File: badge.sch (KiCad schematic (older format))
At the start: 39 parts, among them J1 DevKitC_L, J10 HT024SQV003NH, J11 EXT3, J2 DevKitC_R, J3 HT024SQV010NH, J4 EXT1_1, J5 EXT1_2, J6 EXT1_3, J7 EXT2_1, J8 EXT2_2, J9 EXT2_3, SW1 UP, SW2 LEFT, SW3 A, SW4 DOWN, SW5 RIGHT, SW6 B, SW7 SW_DIP_x03, U1 ESP32-DEVKITC-32D

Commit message: Vertical badge style
* Change C9 footprint to 2816
* Add 3D model for 5 wat tactile switch
* 3D models should be located in ${HOME}/kicad/template
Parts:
- added J13: DevKitC_R_SMD, Connector_PinSocket_2.54mm:PinSocket_1x19_P2.54mm_Vertical_SMD_Pin1Left, symbol Connector:Conn_01x19_Female
- C9: value 0603/220uF/16V -> 2917/220uF/16V; footprint Capacitor_SMD:C_0603_1608Metric -> Capacitor_SMD:C_2816_7142Metric
- SW7: footprint custom_footprint:ITS-1500S -> custom_footprint:ITS-1500S-A
- gave numbers to parts that had none: 1
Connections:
- net GND: now also J13.1 (Pin_1), J13.7 (Pin_7)
- net GPIO15: now also J13.16 (Pin_16)
- net GPIO16: now also J13.12 (Pin_12)
- net GPIO17: now also J13.11 (Pin_11)
- net GPIO2: now also J13.15 (Pin_15)
- net GPIO4: now also J13.13 (Pin_13)
- net LCD_DC: now also J13.3 (Pin_3)
- net LCD_RST: now also J13.6 (Pin_6)
- net VSPI_CS: now also J13.10 (Pin_10)
- net VSPI_MISO: now also J13.8 (Pin_8)
- net VSPI_MOSI: now also J13.2 (Pin_2)
- net VSPI_SCK: now also J13.9 (Pin_9)
- no-connect marks 77 -> 83
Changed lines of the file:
@@
 	5800 500  5800 3200
-Wire Notes Line
-	4100 3200 500  3200
 Wire Notes Line
 	500  3200 500  500
@@
 P 9000 5900
 F 0 "C9" V 8900 5950 50  0000 C CNN
-F 1 "0603/220uF/16V" V 8900 5500 50  0000 C CNN
-F 2 "Capacitor_SMD:C_0603_1608Metric" H 9000 5900 50  0001 C CNN
+F 1 "2917/220uF/16V" V 8900 5500 50  0000 C CNN
+F 2 "Capacitor_SMD:C_2816_7142Metric" H 9000 5900 50  0001 C CNN
 F 3 "~" H 9000 5900 50  0001 C CNN
 	1    9000 5900
@@
 F 0 "SW7" H 4800 5667 50  0000 C CNN
 F 1 "SW_DIP_x03" H 4800 5576 50  0000 C CNN
-F 2 "custom_footprint:ITS-1500S" H 4800 5200 50  0001 C CNN
+F 2 "custom_footprint:ITS-1500S-A" H 4800 5200 50  0001 C CNN
 F 3 "" H 4800 5200 50  0001 C CNN
 	1    4800 5200
@@
 GPIO39
 $Comp
-L Connector:Conn_01x19_Female J?
+L Connector:Conn_01x19_Female J12
 U 1 1 5C04F616
 P 1300 2000
-F 0 "J?" H 1200 3100 50  0000 L CNN
+F 0 "J12" H 1200 3100 50  0000 L CNN
 F 1 "DevKitC_L_SMD" H 1000 3000 50  0000 L CNN
 F 2 "Connector_PinSocket_2.54mm:PinSocket_1x19_P2.54mm_Vertical_SMD_Pin1Right" H 1300 2000 50  0001 C CNN
@@
 NoConn ~ 1100 2600
 $Comp
-L power:+5V #PWR?
+L power:+5V #PWR0117
 U 1 1 5C04F61F
 P 900 2900
-F 0 "#PWR?" H 900 2750 50  0001 C CNN
+F 0 "#PWR0117" H 900 2750 50  0001 C CNN
 F 1 "+5V" H 915 3073 50  0000 C CNN
 F 2 "" H 900 2900 50  0001 C CNN
@@
 GPIO34
 $Comp
-L power:GND #PWR?
+L power:GND #PWR0118
 U 1 1 5C04F628
 P 700 2400
-F 0 "#PWR?" H 700 2150 50  0001 C CNN
+F 0 "#PWR0118" H 700 2150 50  0001 C CNN
 F 1 "GND" H 705 2227 50  0000 C CNN
 F 2 "" H 700 2400 50  0001 C CNN
@@
 	700  2400 1100 2400
 $Comp
-L power:+3.3V #PWR?
+L power:+3.3V #PWR0119
 U 1 1 5C04F62F
 P 700 1100
-F 0 "#PWR?" H 700 950 50  0001 C CNN
+F 0 "#PWR0119" H 700 950 50  0001 C CNN
 F 1 "+3.3V" H 715 1273 50  0000 C CNN
 F 2 "" H 700 1100 50  0001 C CNN
@@
 Text Label 1100 1400 2    50   ~ 0
 GPIO39
+Text Label 5000 1800 0    50   ~ 0
+VSPI_MISO
+Text Label 5000 1200 0    50   ~ 0
+VSPI_MOSI
+Text Label 5000 1900 0    50   ~ 0
+VSPI_SCK
+Text Label 5000 2000 0    50   ~ 0
+VSPI_CS
+Text Label 5000 1300 0    50   ~ 0
+LCD_DC
+$Comp
+L Connector:Conn_01x19_Female J13
+U 1 1 5C053B91
+P 4800 2000
+F 0 "J13" H 4694 3085 50  0000 C CNN
+F 1 "DevKitC_R_SMD" H 4694 2994 50  0000 C CNN
+F 2 "Connector_PinSocket_2.54mm:PinSocket_1x19_P2.54mm_Vertical_SMD_Pin1Left" H 4800 2000 50  0001 C CNN
+F 3 "~" H 4800 2000 50  0001 C CNN
+	1    4800 2000
+	-1   0    0    -1
+$EndComp
+Text Label 5000 1600 0    50   ~ 0
+LCD_RST
+NoConn ~ 5000 1400
+NoConn ~ 5000 1500
+NoConn ~ 5000 2700
+NoConn ~ 5000 2800
+NoConn ~ 5000 2900
+$Comp
+L power:GND #PWR0120
+U 1 1 5C053B9E
+P 5500 1100
+F 0 "#PWR0120" H 5500 850 50  0001 C CNN
+F 1 "GND" H 5505 927 50  0000 C CNN
+F 2 "" H 5500 1100 50  0001 C CNN
+F 3 "" H 5500 1100 50  0001 C CNN
+	1    5500 1100
+	1    0    0    -1
+$EndComp
+$Comp
+L power:GND #PWR0121
+U 1 1 5C053BA4
+P 5500 1700
+F 0 "#PWR0121" H 5500 1450 50  0001 C CNN
+F 1 "GND" H 5505 1527 50  0000 C CNN
+F 2 "" H 5500 1700 50  0001 C CNN
+F 3 "" H 5500 1700 50  0001 C CNN
+	1    5500 1700
+	1    0    0    -1
+$EndComp
+Wire Wire Line
+	5000 1700 5500 1700
+Wire Wire Line
+	5000 1100 5500 1100
+Text Label 5000 2300 0    50   ~ 0
+GPIO4
+Text Label 5000 2600 0    50   ~ 0
+GPIO15
+Text Label 5000 2200 0    50   ~ 0
+GPIO16
+Text Label 5000 2100 0    50   ~ 0
+GPIO17
+Text Label 5000 2500 0    50   ~ 0
+GPIO2
+NoConn ~ 5000 2400
+Wire Notes Line
+	500  3200 5000 3200
 $EndSCHEMATC

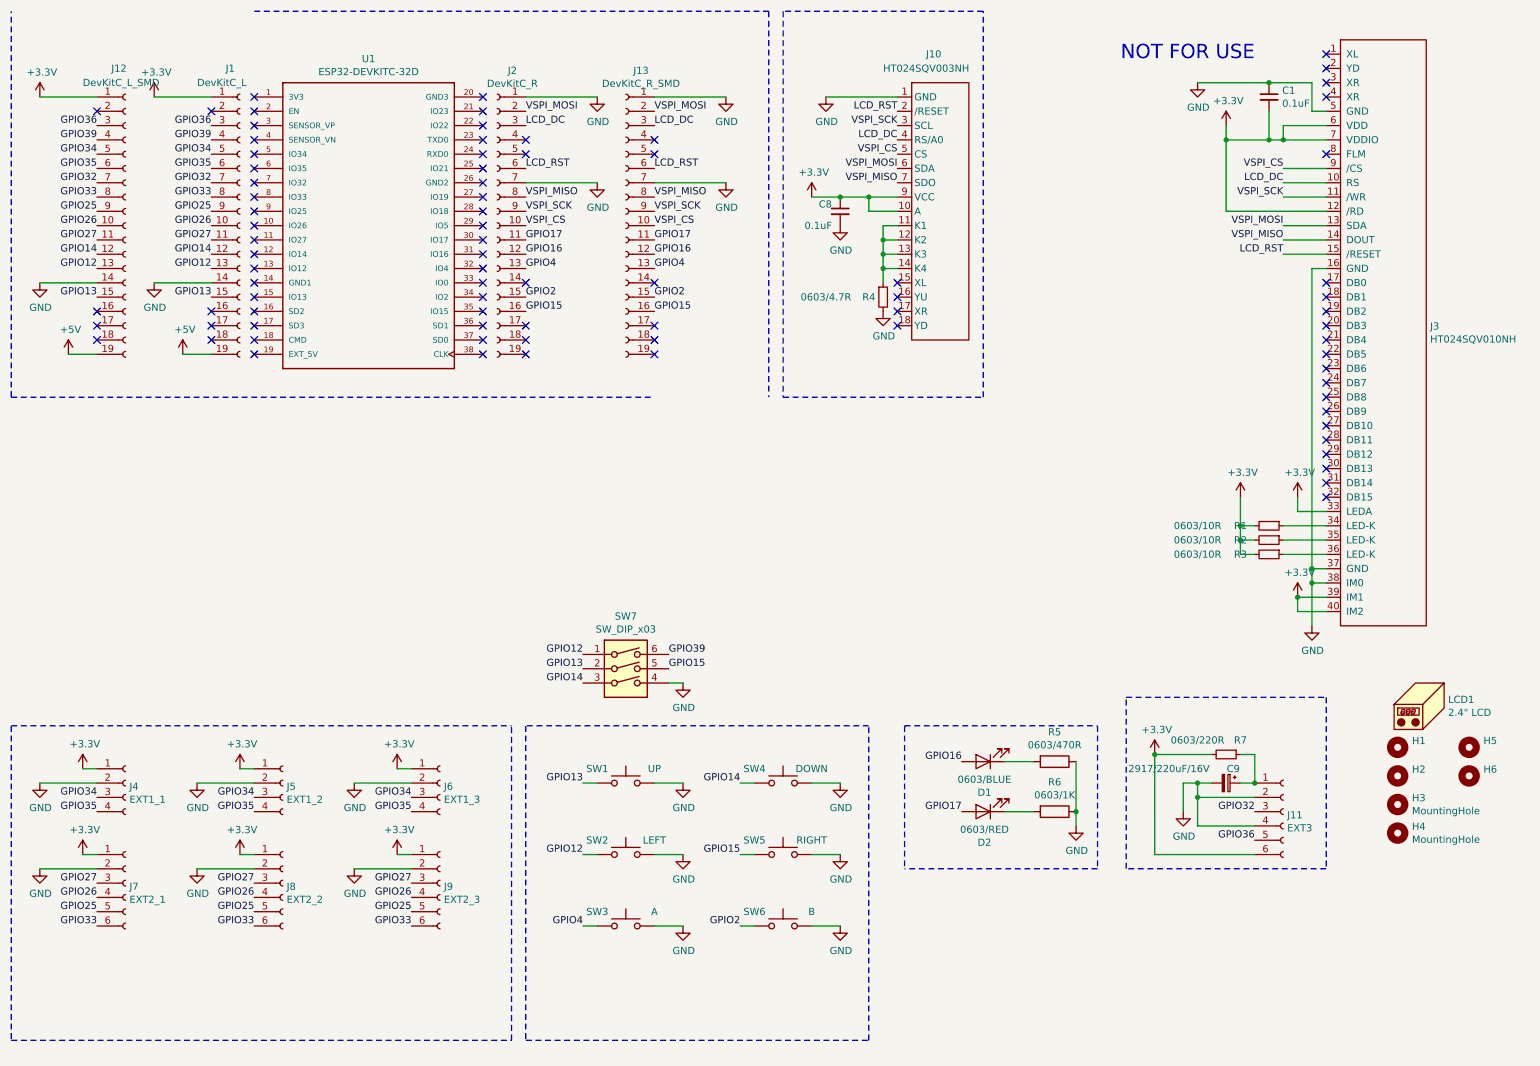
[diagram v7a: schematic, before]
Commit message: Modify footprints for Silk, add IR333C
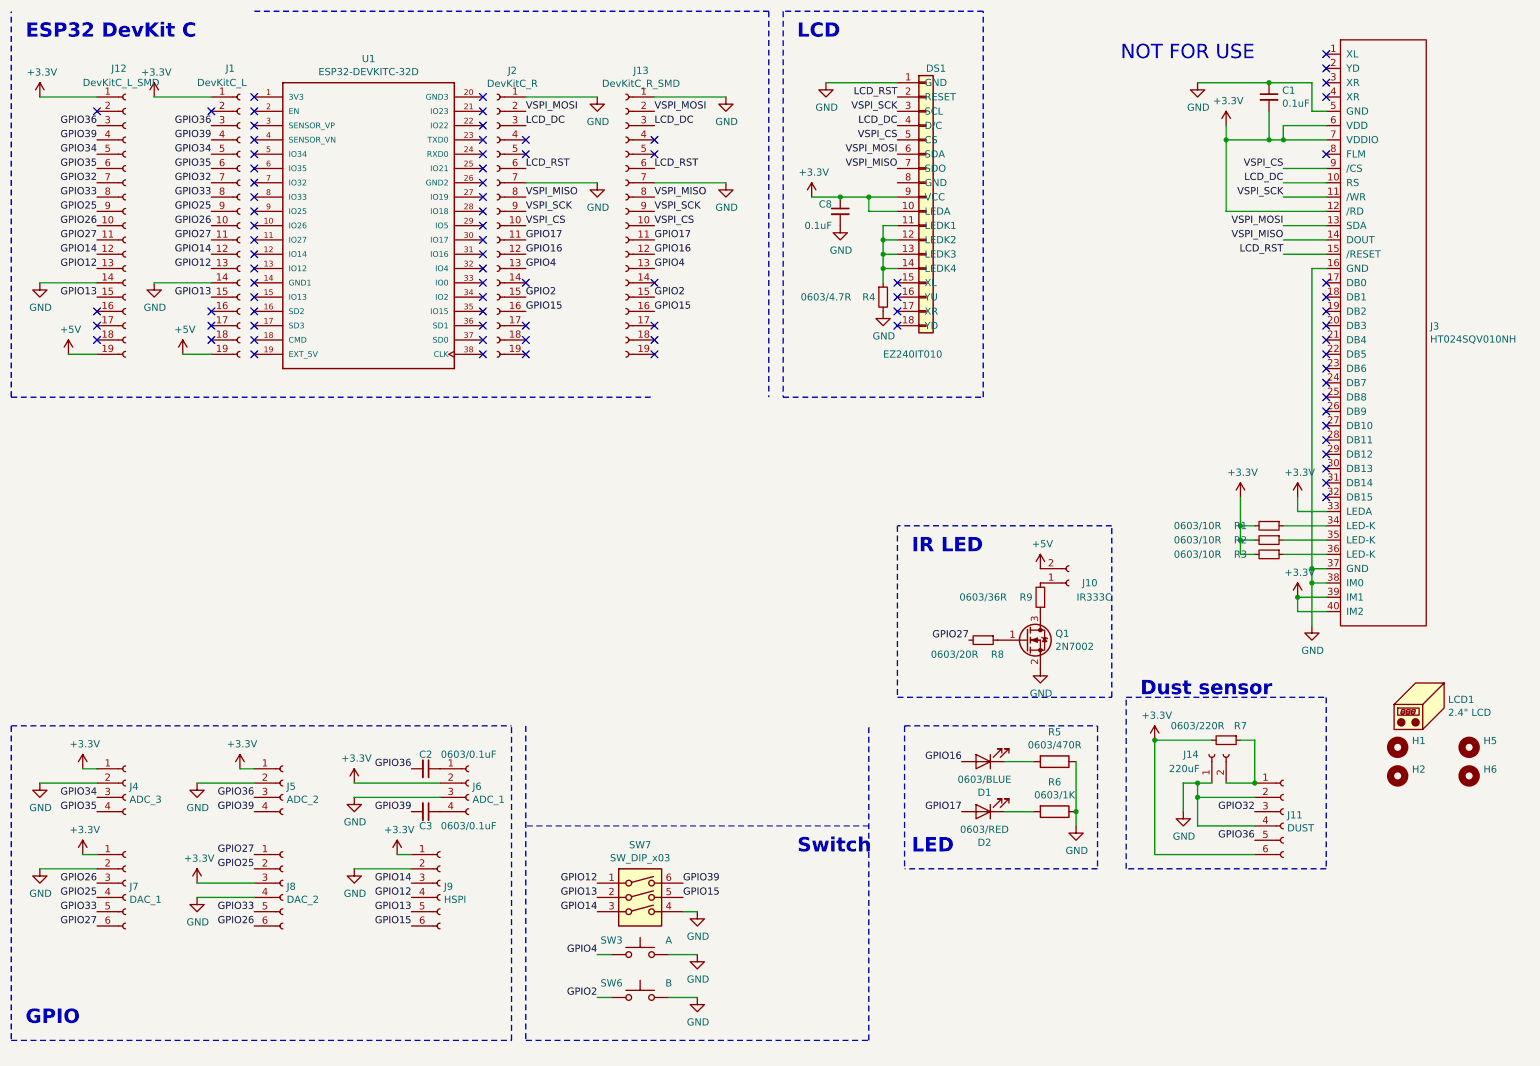
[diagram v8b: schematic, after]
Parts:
- removed C9: 2917/220uF/16V, Capacitor_SMD:C_2816_7142Metric, symbol Device:CP_Small
- removed H3, H4: MountingHole, MountingHole:MountingHole_8.4mm_M8, symbol Mechanical:MountingHole
- removed J10: HT024SQV003NH, custom_footprint:COMMON_MOUNT_FFC-1x18-1MP_P0.80mm, symbol New_Library:HT024SQV003NH
- removed SW1: UP, Button_Switch_SMD:SW_SPST_TL3342, symbol Switch:SW_Push
- removed SW2: LEFT, Button_Switch_SMD:SW_SPST_TL3342, symbol Switch:SW_Push
- removed SW4: DOWN, Button_Switch_SMD:SW_SPST_TL3342, symbol Switch:SW_Push
- removed SW5: RIGHT, Button_Switch_SMD:SW_SPST_TL3342, symbol Switch:SW_Push
- added C2, C3: 0603/0.1uF, Capacitor_SMD:C_0603_1608Metric, symbol Device:C_Small
- added DS1: EZ240IT010, custom_footprint:COMMON_MOUNT_FFC-1x18-1MP_P0.80mm, symbol New_Library:LCD_SPI_18P
- added J10: IR333C, custom_footprint:PinSocket_1x02_P2.54mm_Vertical_NO3D, symbol Connector:Conn_01x02_Female
- added J14: 220uF, custom_footprint:PinSocket_1x02_P2.54mm_Vertical_NO3D, symbol Connector:Conn_01x02_Female
- added Q1: 2N7002, Package_TO_SOT_SMD:SOT-23, symbol Transistor_FET:2N7002
- added R8: 0603/20R, Resistor_SMD:R_0603_1608Metric, symbol Device:R_Small
- added R9: 0603/36R, Resistor_SMD:R_0603_1608Metric, symbol Device:R_Small
- J11: value EXT3 -> DUST
- J4: value EXT1_1 -> ADC_3; footprint custom_footprint:PinSocket_1x04_P2.54mm_Vertical_NO3D -> custom_footprint:PinSocket_1x04_P2.54mm_Vertical_NO3D_1S
- J5: value EXT1_2 -> ADC_2; footprint custom_footprint:PinSocket_1x04_P2.54mm_Vertical_NO3D -> custom_footprint:PinSocket_1x04_P2.54mm_Vertical_NO3D_1S
- J6: value EXT1_3 -> ADC_1; footprint custom_footprint:PinSocket_1x04_P2.54mm_Vertical_NO3D -> custom_footprint:PinSocket_1x04_P2.54mm_Vertical_NO3D_2S
- J7: value EXT2_1 -> DAC_1; footprint custom_footprint:PinSocket_1x06_P2.54mm_Vertical_NO3D -> custom_footprint:PinSocket_1x06_P2.54mm_Vertical_NO3D_1S
- J8: value EXT2_2 -> DAC_2; footprint custom_footprint:PinSocket_1x06_P2.54mm_Vertical_NO3D -> custom_footprint:PinSocket_1x06_P2.54mm_Vertical_NO3D_3S
- J9: value EXT2_3 -> HSPI; footprint custom_footprint:PinSocket_1x06_P2.54mm_Vertical_NO3D -> custom_footprint:PinSocket_1x06_P2.54mm_Vertical_NO3D_5S
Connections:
- net +3V3: now also J6.2 (Pin_2), J8.3 (Pin_3), DS1.10 (LEDA), DS1.9 (VCC); no longer J6.1 (Pin_1), J8.1 (Pin_1)
- net +5V: now also J10.2 (Pin_2)
- net GND: now also J6.3 (Pin_3), J8.4 (Pin_4), DS1.1 (GND), J14.1 (Pin_1), Q1.2 (S); no longer J6.2 (Pin_2), J8.2 (Pin_2)
- net GPIO12: now also J9.4 (Pin_4)
- net GPIO13: now also J9.5 (Pin_5)
- net GPIO14: now also J9.3 (Pin_3)
- net GPIO15: now also J9.6 (Pin_6)
- net GPIO25: now also J7.4 (Pin_4), J8.2 (Pin_2); no longer J7.5 (Pin_5), J8.5 (Pin_5), J9.5 (Pin_5)
- net GPIO26: now also J7.3 (Pin_3), J8.6 (Pin_6); no longer J7.4 (Pin_4), J8.4 (Pin_4), J9.4 (Pin_4)
- net GPIO27: now also J7.6 (Pin_6), J8.1 (Pin_1), R8.2; no longer J7.3 (Pin_3), J8.3 (Pin_3), J9.3 (Pin_3)
- net GPIO33: now also J7.5 (Pin_5), J8.5 (Pin_5); no longer J7.6 (Pin_6), J8.6 (Pin_6), J9.6 (Pin_6)
- net GPIO34: no longer J5.3 (Pin_3), J6.3 (Pin_3)
- net GPIO35: no longer J5.4 (Pin_4), J6.4 (Pin_4)
- net GPIO36: now also J5.3 (Pin_3), C2.2
- net GPIO39: now also J5.4 (Pin_4), C3.2
- net LCD_DC: now also DS1.4 (D/C)
- net LCD_RST: now also DS1.2 (RESET)
- net VSPI_CS: now also DS1.5 (CS)
- net VSPI_MISO: now also DS1.7 (SDO)
- net VSPI_MOSI: now also DS1.6 (SDA)
- net VSPI_SCK: now also DS1.3 (SCL)
- net at R4.1: now also DS1.11 (LEDK1), DS1.12 (LEDK2), DS1.13 (LEDK3), DS1.14 (LEDK4)
- net at J11.1 (Pin_1), R7.1: now also J14.2 (Pin_2)
- new net: C2.1, J6.1 (Pin_1)
- new net: C3.1, J6.4 (Pin_4)
- new net: Q1.1 (G), R8.1
- new net: Q1.3 (D), R9.1
- new net: J10.1 (Pin_1), R9.2
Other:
- note added: "Dust sensor"
- note added: "ESP32 DevKit C"
- note added: "GPIO"
- note added: "IR LED\n"
- note added: "LCD"
- note added: "LED\n"
- note added: "Switch"
- moved on the sheet: J6, R7, SW3, SW6, SW7
